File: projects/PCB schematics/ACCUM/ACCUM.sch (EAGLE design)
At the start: 14 parts, among them IC2 78L08SMD, Q2 IRLZ44Z

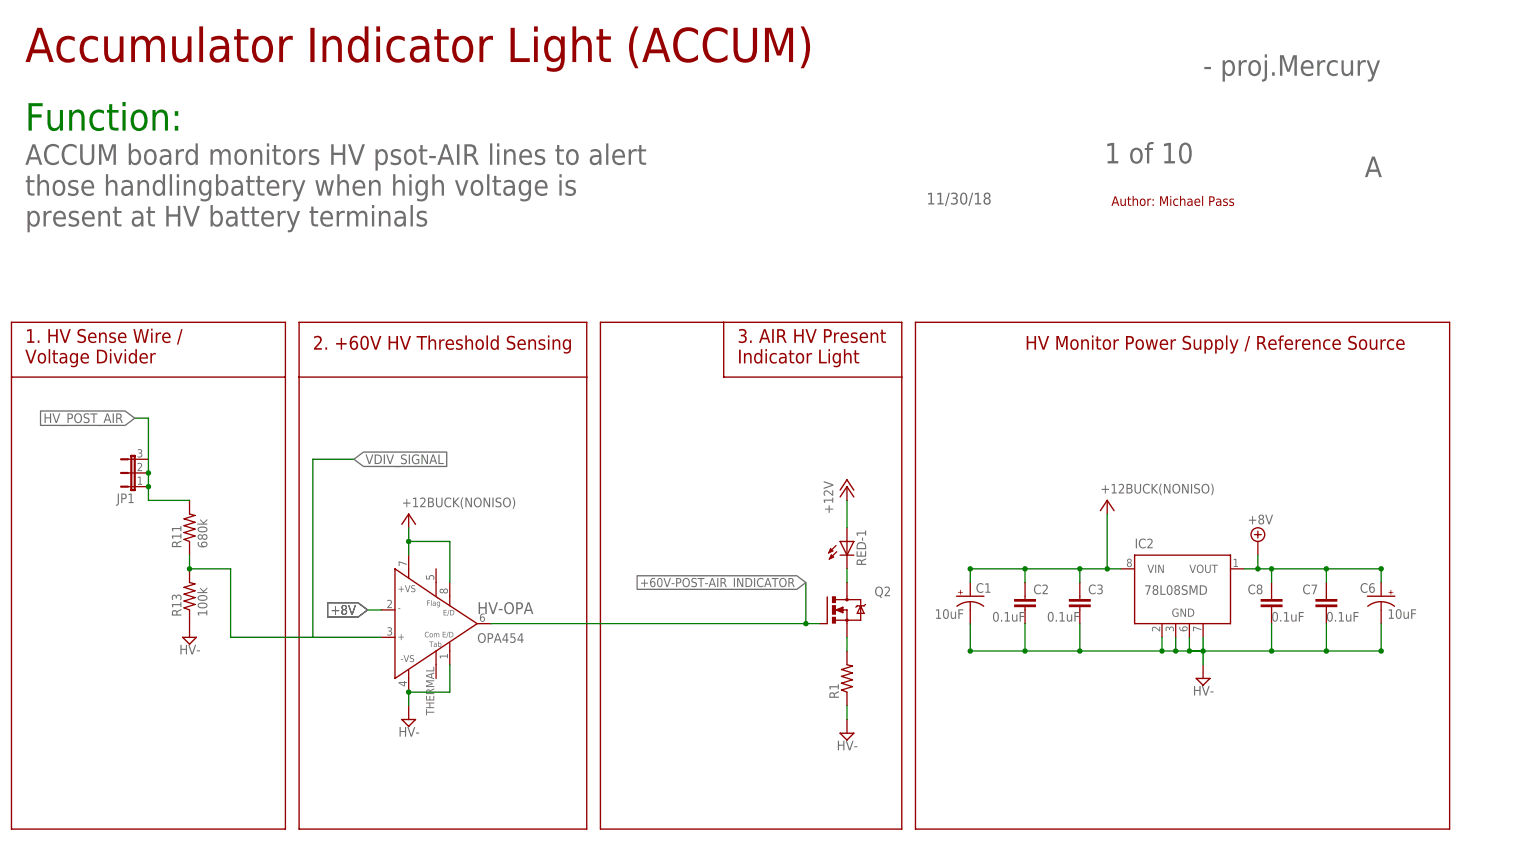
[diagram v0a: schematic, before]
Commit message: SC - Rev A; First PCB revision complete.
This marks the first draft of the SC board.
Parts have been laid out and initial routing completed through
extensive use of autorouter.
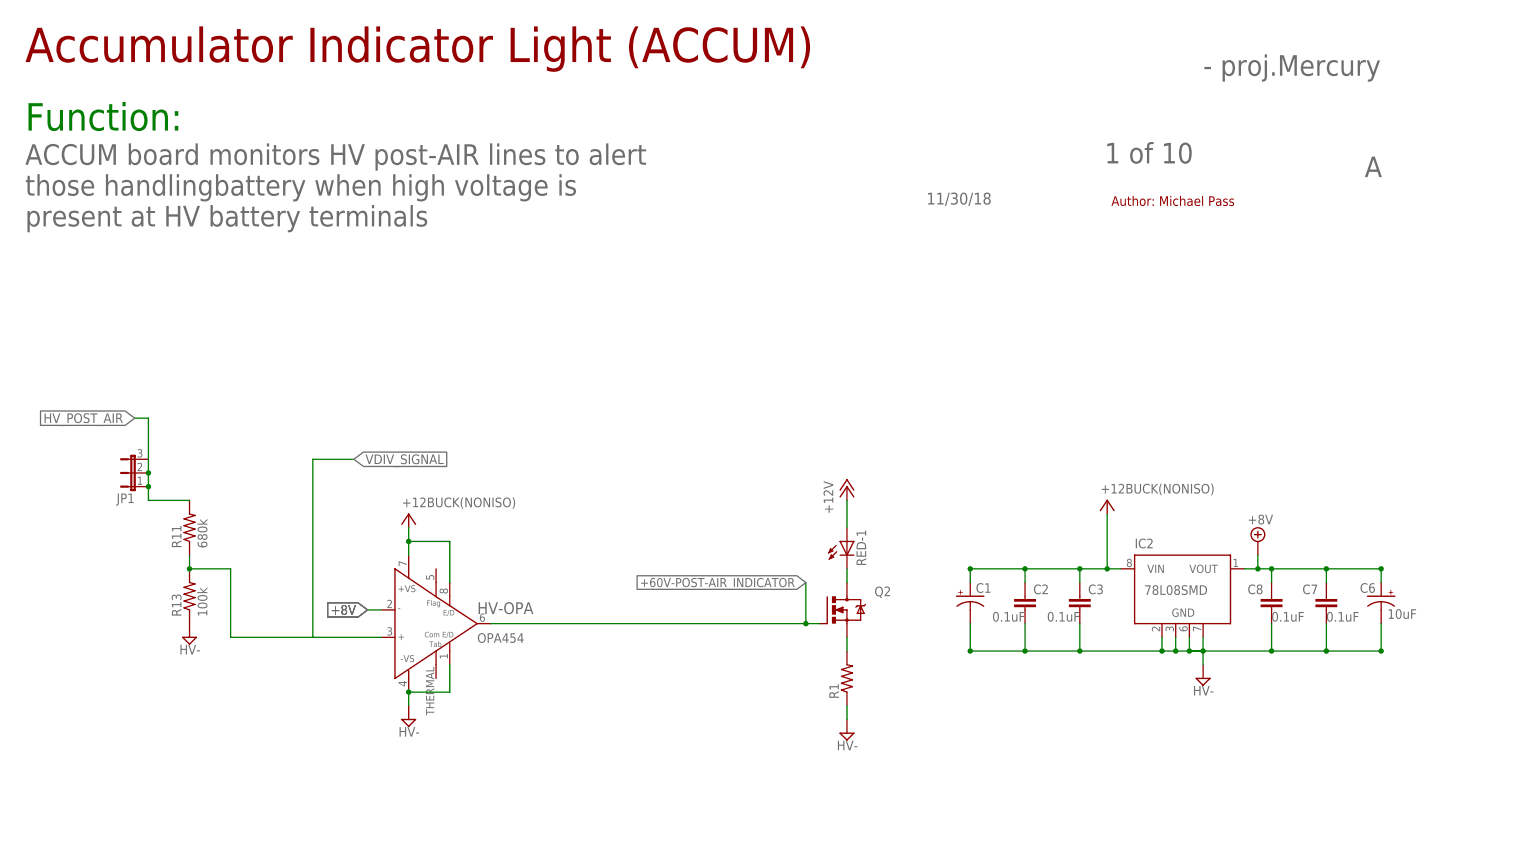
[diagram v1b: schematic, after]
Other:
- note added: "ACCUM board monitors HV post-AIR lines to alert those handlingbattery when high voltage is present at HV battery terminals"
- note removed: "1. HV Sense Wire / Voltage Divider"
- note removed: "2. +60V HV Threshold Sensing"
- note removed: "3. AIR HV Present Indicator Light"
- note removed: "ACCUM board monitors HV psot-AIR lines to alert those handlingbattery when high voltage is present at HV battery terminals"
- note removed: "HV Monitor Power Supply / Reference Source"
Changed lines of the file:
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@@
 <?xml version="1.0" encoding="utf-8"?>
 <!DOCTYPE eagle SYSTEM "eagle.dtd">
-<eagle version="9.3.0">
+<eagle version="9.3.1">
 <drawing>
 <settings>
@@
 <sheet>
 <plain>
-<text x="63.5" y="93.98" size="2.54" layer="94">2. +60V HV Threshold Sensing</text>
-<frame x1="193.04" y1="91.44" x2="274.32" y2="99.06" columns="8" rows="5" layer="94" border-left="no" border-top="no" border-right="no" border-bottom="no"/>
-<text x="10.16" y="91.44" size="2.54" layer="94">1. HV Sense Wire /
-Voltage Divider</text>
-<text x="195.58" y="93.98" size="2.54" layer="94">HV Monitor Power Supply / Reference Source</text>
-<text x="142.24" y="91.44" size="2.54" layer="94">3. AIR HV Present
-Indicator Light</text>
 <text x="10.16" y="147.32" size="6.35" layer="94">Accumulator Indicator Light (ACCUM)</text>
 <text x="10.16" y="134.62" size="5.08" layer="91">Function:</text>
@@
 <text x="210.312" y="128.524" size="3.81" layer="96">1 of 10</text>
 <text x="228.6" y="144.78" size="3.81" layer="96">- proj.Mercury</text>
-<text x="10.16" y="116.84" size="3.81" layer="96">ACCUM board monitors HV psot-AIR lines to alert
+<text x="10.16" y="116.84" size="3.81" layer="96">ACCUM board monitors HV post-AIR lines to alert
 those handlingbattery when high voltage is
 present at HV battery terminals</text>
 <text x="211.582" y="120.65" size="1.778" layer="94">Author: Michael Pass</text>
 <text x="258.572" y="125.984" size="3.81" layer="96">A</text>
-<wire x1="7.62" y1="5.08" x2="7.62" y2="88.9" width="0.254" layer="94"/>
-<wire x1="7.62" y1="88.9" x2="7.62" y2="99.06" width="0.254" layer="94"/>
-<wire x1="7.62" y1="99.06" x2="58.42" y2="99.06" width="0.254" layer="94"/>
-<wire x1="58.42" y1="99.06" x2="58.42" y2="88.9" width="0.254" layer="94"/>
-<wire x1="58.42" y1="88.9" x2="58.42" y2="5.08" width="0.254" layer="94"/>
-<wire x1="58.42" y1="5.08" x2="7.62" y2="5.08" width="0.254" layer="94"/>
-<wire x1="60.96" y1="88.9" x2="60.96" y2="5.08" width="0.254" layer="94"/>
-<wire x1="60.96" y1="5.08" x2="114.3" y2="5.08" width="0.254" layer="94"/>
-<wire x1="114.3" y1="5.08" x2="114.3" y2="88.9" width="0.254" layer="94"/>
-<wire x1="114.3" y1="88.9" x2="114.3" y2="99.06" width="0.254" layer="94"/>
-<wire x1="114.3" y1="99.06" x2="60.96" y2="99.06" width="0.254" layer="94"/>
-<wire x1="116.84" y1="99.06" x2="116.84" y2="5.08" width="0.254" layer="94"/>
-<wire x1="116.84" y1="5.08" x2="172.72" y2="5.08" width="0.254" layer="94"/>
-<wire x1="172.72" y1="5.08" x2="172.72" y2="88.9" width="0.254" layer="94"/>
-<wire x1="172.72" y1="88.9" x2="172.72" y2="99.06" width="0.254" layer="94"/>
-<wire x1="172.72" y1="99.06" x2="139.7" y2="99.06" width="0.254" layer="94"/>
-<wire x1="139.7" y1="99.06" x2="116.84" y2="99.06" width="0.254" layer="94"/>
-<wire x1="175.26" y1="99.06" x2="175.26" y2="5.08" width="0.254" layer="94"/>
-<wire x1="175.26" y1="5.08" x2="274.32" y2="5.08" width="0.254" layer="94"/>
-<wire x1="274.32" y1="5.08" x2="274.32" y2="99.06" width="0.254" layer="94"/>
-<wire x1="274.32" y1="99.06" x2="175.26" y2="99.06" width="0.254" layer="94"/>
-<wire x1="60.96" y1="99.06" x2="60.96" y2="88.9" width="0.254" layer="94"/>
-<wire x1="60.96" y1="88.9" x2="114.3" y2="88.9" width="0.254" layer="94"/>
-<wire x1="58.42" y1="88.9" x2="7.62" y2="88.9" width="0.254" layer="94"/>
-<wire x1="139.7" y1="99.06" x2="139.7" y2="88.9" width="0.254" layer="94"/>
-<wire x1="139.7" y1="88.9" x2="172.72" y2="88.9" width="0.254" layer="94"/>
-<frame x1="0" y1="0" x2="279.4" y2="170.18" columns="8" rows="5" layer="91"/>
 </plain>
 <instances>
@@
 <instance part="C1" gate="G$1" x="185.42" y="48.26" smashed="yes">
 <attribute name="NAME" x="186.436" y="48.895" size="1.778" layer="95"/>
-<attribute name="VALUE" x="178.816" y="44.069" size="1.778" layer="96"/>
 </instance>
 <instance part="C2" gate="G$1" x="195.58" y="48.26" smashed="yes">
